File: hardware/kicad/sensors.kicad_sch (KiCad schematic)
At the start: 6 parts, among them J3 JST SM06B-GHS-TB (SEN66-SIN-T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, J4 1x5 P1.27mm through-hole head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, U4 MIKROE-2462 NFC Tag 2 Click (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

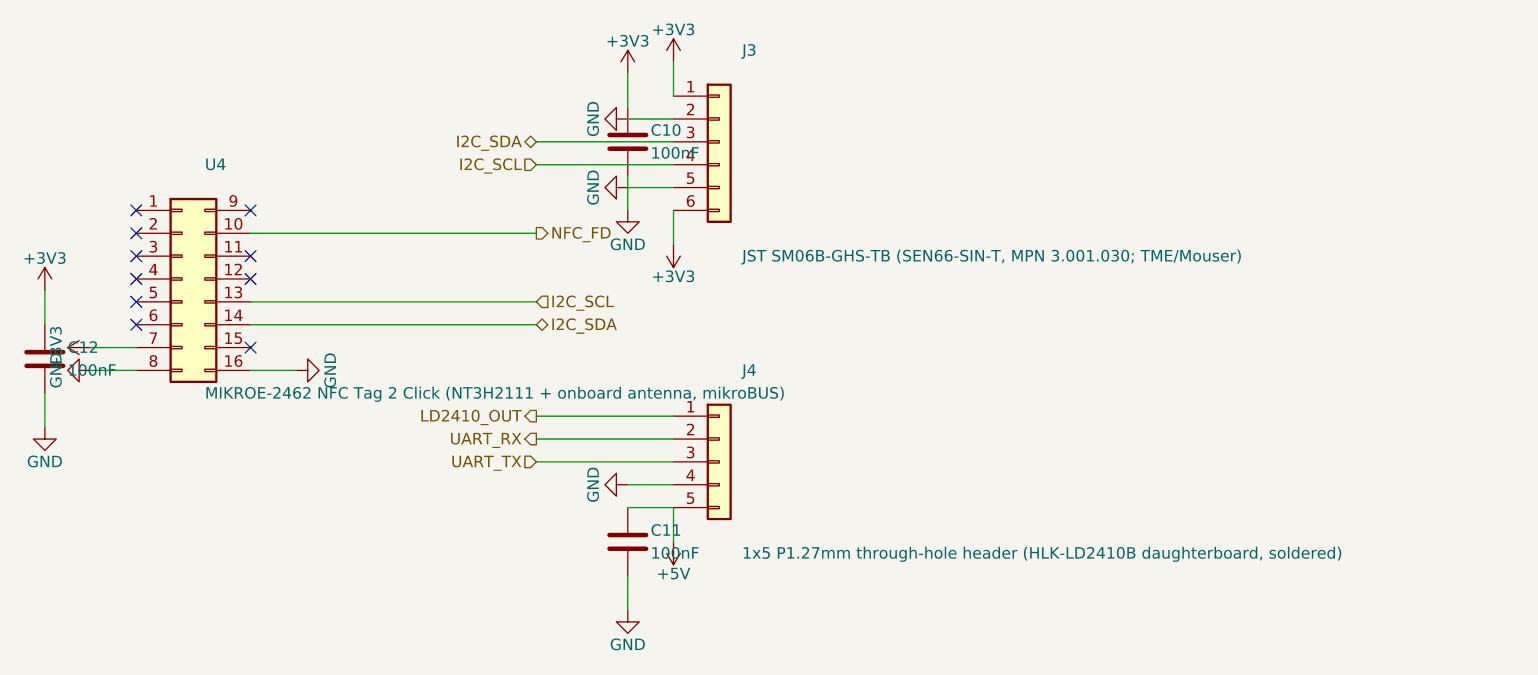
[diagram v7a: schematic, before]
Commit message: docs+kicad: NT3H2111 -> NT3H1101 chip ID + clear v0.6 PCB-mount text
Three documentation cleanups from independent code review:

Task #5 (mikroe-2462.md): the MIKROE-2462 production board carries
NXP NT3H1101 (NTAG I2C, 888 bytes EEPROM), confirmed via the official
MikroE datasheet PDF (PID MIKROE-2462, dated 2017-02-24) and TME
catalog ("Comp: NT3H1101"). MikroE's product page text mentions
"NT3H2111" but the datasheet code example writes 888 bytes of user
memory which matches NT3H1101, not NT3H2111. Both chips share I2C
address 0x55 and the FD interrupt pin, so firmware is unaffected.
Updated all generate.py descr strings and CLAUDE.md references.

Task #7: stale SEN66 cover-mount text in generate.py (lines 121-129,
702-703, 962, 1135, 1148, 1170, 1215, 1511, 1541, 2672) referenced
the pre-v0.6 plan where the SEN66 mounted inside the AK-N-94 cover.
v0.6 reversed that decision (SEN66 PCB-mounted face-up). Comments
and footprint descr/tags now reflect the current architecture.

Task #6 (CLAUDE.md pinout table line 162): I2C pull-ups corrected
from "4.7 kOhm" to "10 kOhm" — matches the schematic (R5/R6 in
gen_mcu_sch) and the SEN66 datasheet section 3.1 spec. v0.6
changelog already records the bump; the pinout table just hadn't
been re-synced.

DRC=0, ERC=0. No PCB geometry change.

Co-Authored-By: Claude Opus 4.7 (1M context) <noreply@anthropic.com>
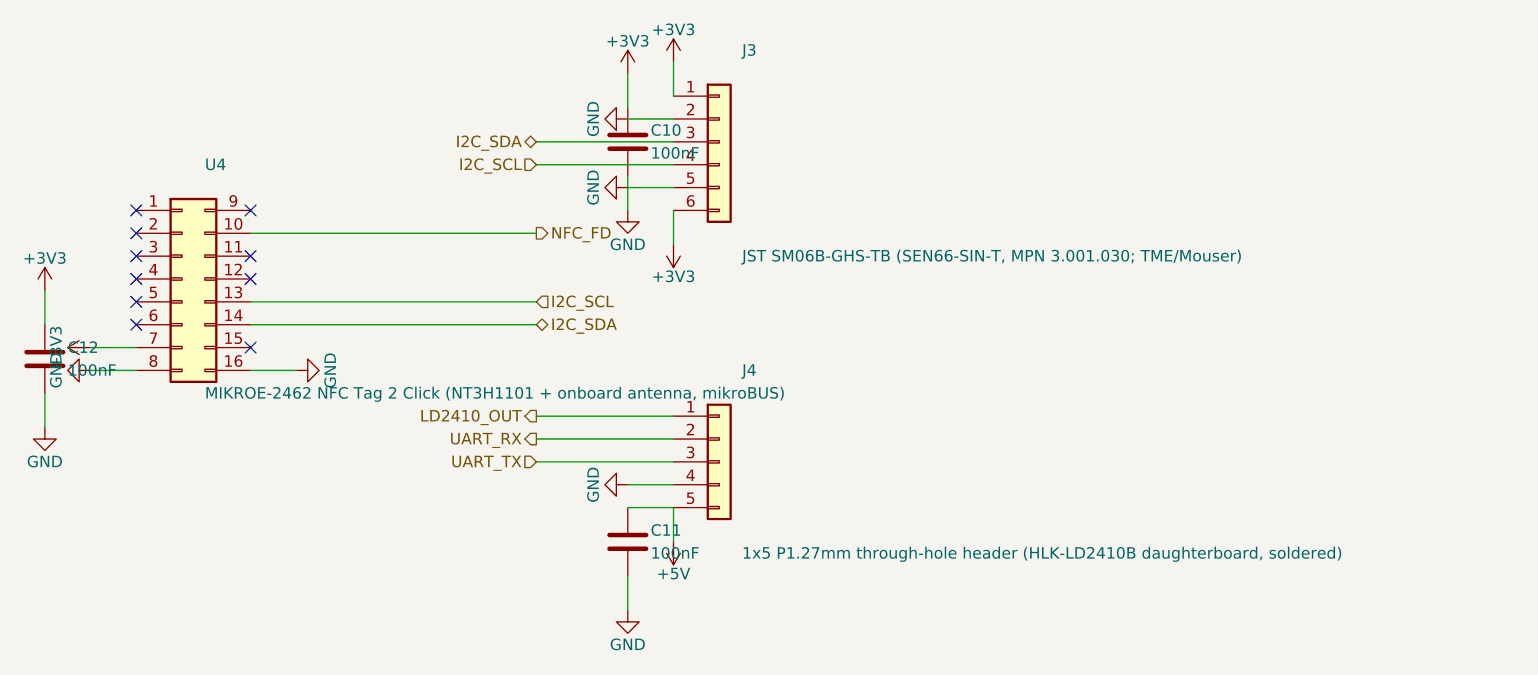
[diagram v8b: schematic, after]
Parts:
- U4: value MIKROE-2462 NFC Tag 2 Click (NT3H2111 + onboard antenna, mikroBUS) -> MIKROE-2462 NFC Tag 2 Click (NT3H1101 + onboard antenna, mikroBUS)
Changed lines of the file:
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@@
         			)
         		)
-        		(property "Value" "MIKROE-2462 NFC Tag 2 Click (NT3H2111 + onboard antenna, mikroBUS)"
+        		(property "Value" "MIKROE-2462 NFC Tag 2 Click (NT3H1101 + onboard antenna, mikroBUS)"
         			(at 123.19 138.43 0)
         			(effects
@@
         			)
         		)
-        		(property "Description" "mikroBUS 2x8 socket — MIKROE-2462 NFC Tag 2 Click daughterboard (NT3H2111 NTAG I²C plus + onboard PCB antenna)"
+        		(property "Description" "mikroBUS 2x8 socket — MIKROE-2462 NFC Tag 2 Click daughterboard (NT3H1101 NTAG I²C plus + onboard PCB antenna)"
         			(at 120.65 125.73 0)
         			(effects
